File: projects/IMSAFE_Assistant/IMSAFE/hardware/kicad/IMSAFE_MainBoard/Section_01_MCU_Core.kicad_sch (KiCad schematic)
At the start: 0 parts

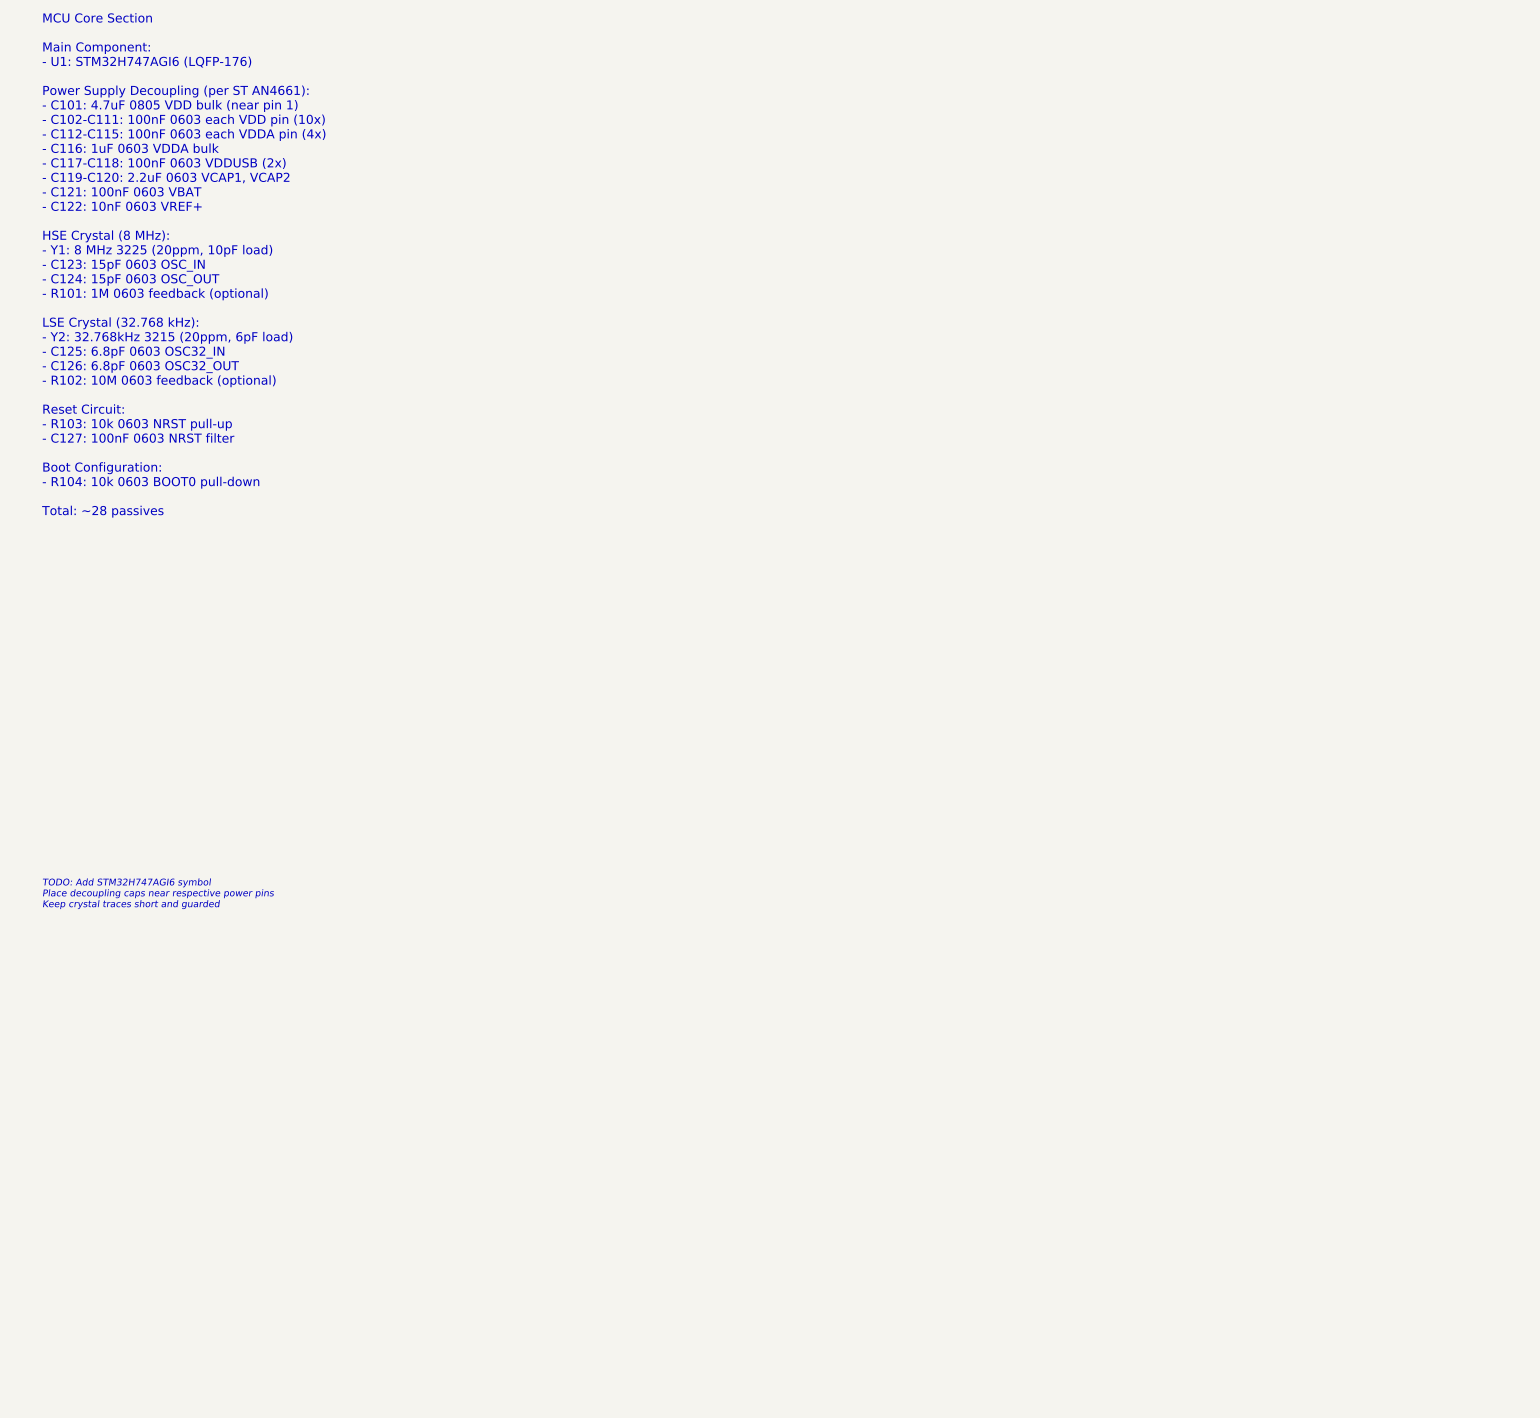
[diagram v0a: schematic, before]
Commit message: Add schematic circuits for MCU, USB-C, and Charger sections
Section 01 (MCU Core):
- STM32H747 decoupling network (22 caps per AN4661)
- HSE 8MHz and LSE 32.768kHz crystal circuits
- Reset circuit with pull-up and filter
- BOOT0 pull-down for flash boot

Section 02 (USB-C Input):
- USB-C 16-pin receptacle with CC resistors (UFP sink)
- USBLC6-2SC6 ESD protection on D+/D-
- VBUS filtering (100nF + 10uF)

Section 03 (Battery Charger):
- BQ25792 buck-boost charger with NVDC power-path
- 2.2uH power inductor
- Input, output, and system capacitors
- Current sense resistors and I2C pull-ups

Co-Authored-By: Claude Opus 4.5 <noreply@anthropic.com>
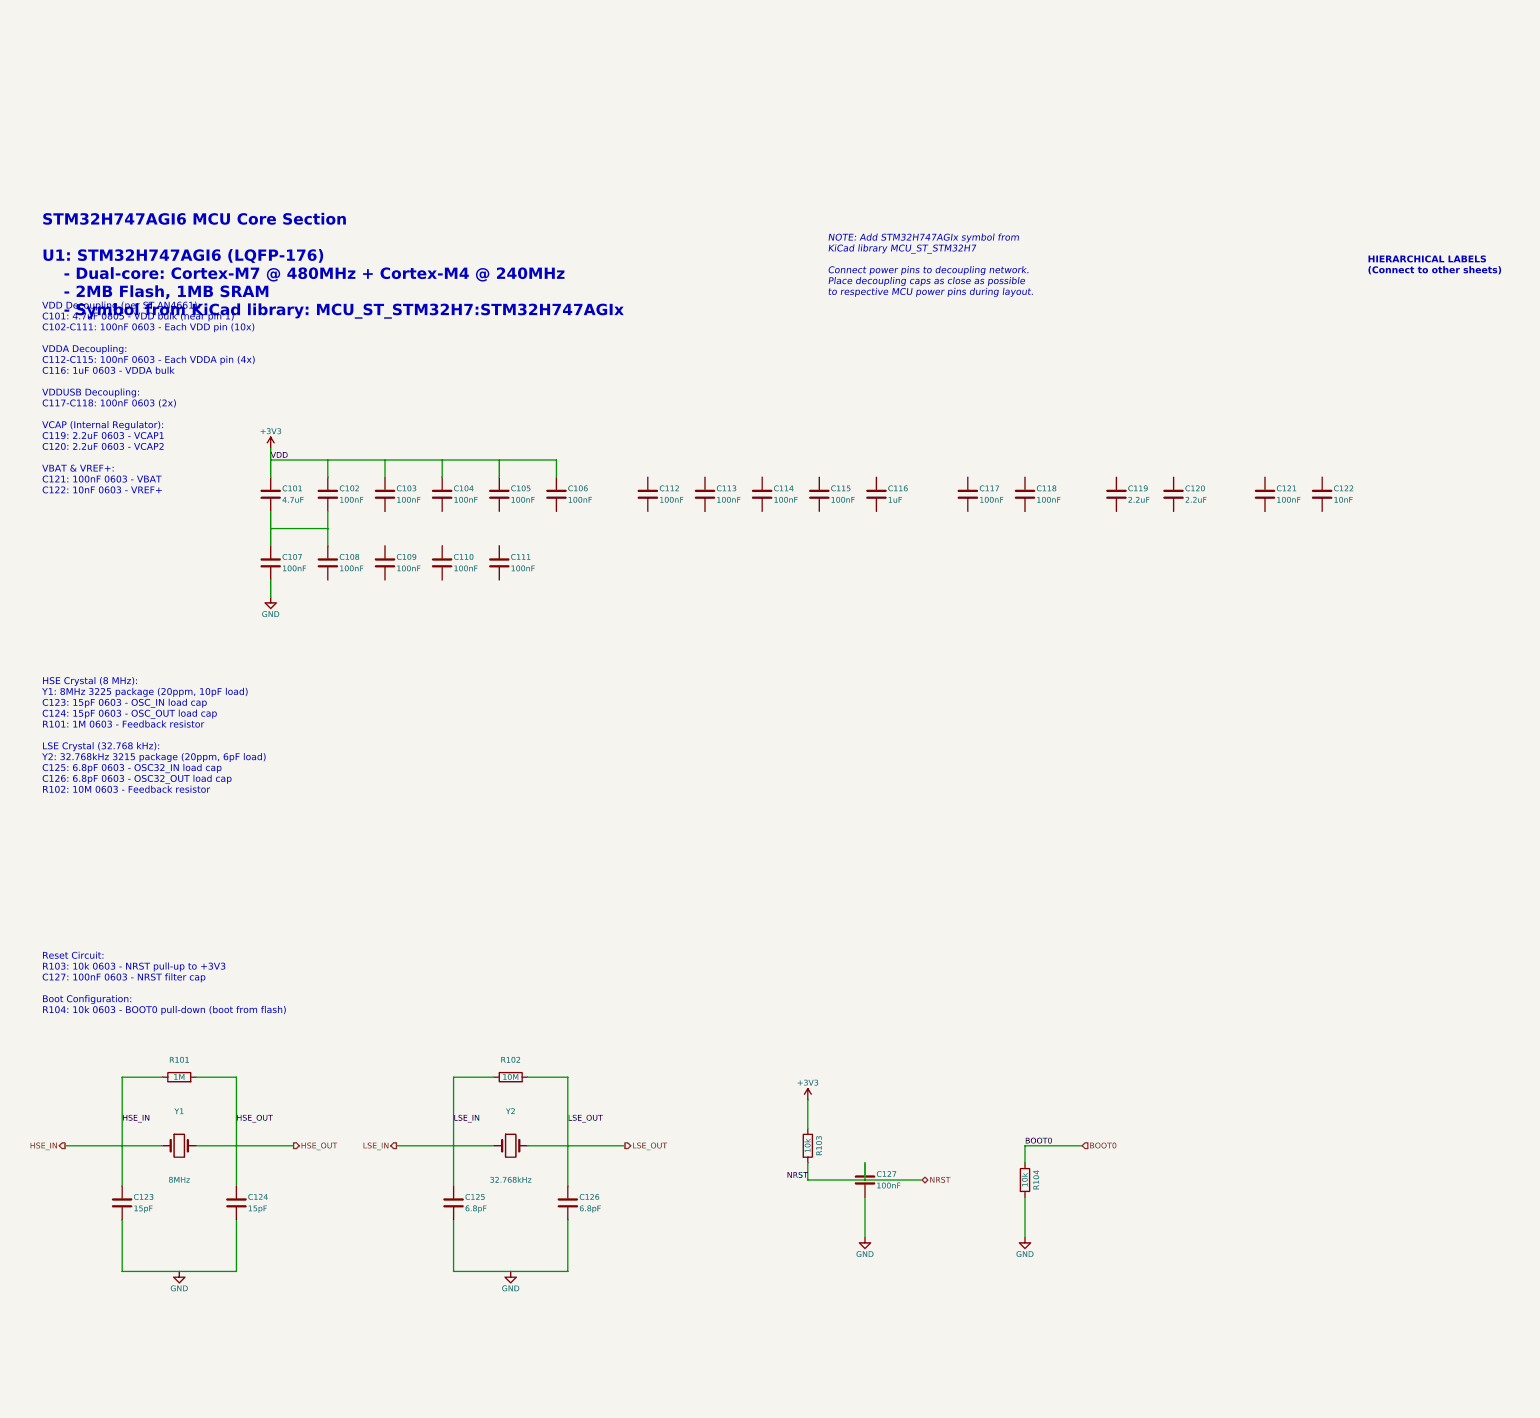
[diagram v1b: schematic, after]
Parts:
- added C101: 4.7uF, Capacitor_SMD:C_0805_2012Metric, symbol Device:C
- added C102, C103, C104, C105, C106, C107, C108, C109, C110, C111, C112, C113, C114, C115, C117, C118, C121, C127: 100nF, Capacitor_SMD:C_0603_1608Metric, symbol Device:C
- added C116: 1uF, Capacitor_SMD:C_0603_1608Metric, symbol Device:C
- added C119, C120: 2.2uF, Capacitor_SMD:C_0603_1608Metric, symbol Device:C
- added C122: 10nF, Capacitor_SMD:C_0603_1608Metric, symbol Device:C
- added C123, C124: 15pF, Capacitor_SMD:C_0603_1608Metric, symbol Device:C
- added C125, C126: 6.8pF, Capacitor_SMD:C_0603_1608Metric, symbol Device:C
- added R101: 1M, Resistor_SMD:R_0603_1608Metric, symbol Device:R
- added R102: 10M, Resistor_SMD:R_0603_1608Metric, symbol Device:R
- added R103, R104: 10k, Resistor_SMD:R_0603_1608Metric, symbol Device:R
- added Y1: 8MHz, Crystal:Crystal_SMD_3225-4Pin_3.2x2.5mm, symbol Device:Crystal
- added Y2: 32.768kHz, Crystal:Crystal_SMD_3215-2Pin_3.2x1.5mm, symbol Device:Crystal
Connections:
- new net: C101.2, C102.2, C107.1, C108.1
- new net +3V3: C101.1, C106.1, R103.1
- new net BOOT0: R104.1
- new net GND: C107.2, C123.2, C124.2, C125.2, C126.2, C127.2, R104.2
- new net HSE_IN: C123.1, R101.1, Y1.1
- new net HSE_OUT: C124.1, R101.2, Y1.2
- new net LSE_IN: C125.1, R102.1, Y2.1
- new net LSE_OUT: C126.1, R102.2, Y2.2
- new net NRST: C127.1, R103.2
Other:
- note added: "HIERARCHICAL LABELS (Connect to other sheets)"
- note added: "HSE Crystal (8 MHz): Y1: 8MHz 3225 package (20ppm, 10pF load) C123: 15pF 0603 - OSC_IN load cap C124: 15pF 0603 - OSC_OUT load cap R101: 1M 0603 - Feedback resistor LSE Crystal (32.768 kHz): Y2: 32.768kHz 3215 package (20ppm, 6pF load) C125: 6.8pF 0603 - OSC32_IN load cap C126: 6.8pF 0603 - OSC32_OUT load cap R102: 10M 0603 - Feedback resistor"
- note added: "NOTE: Add STM32H747AGIx symbol from KiCad library MCU_ST_STM32H7 Connect power pins to decoupling network. Place decoupling caps as close as possible to respective MCU power pins during layout."
- note added: "Reset Circuit: R103: 10k 0603 - NRST pull-up to +3V3 C127: 100nF 0603 - NRST filter cap Boot Configuration: R104: 10k 0603 - BOOT0 pull-down (boot from flash)"
- note added: "STM32H747AGI6 MCU Core Section U1: STM32H747AGI6 (LQFP-176) - Dual-core: Cortex-M7 @ 480MHz + Cortex-M4 @ 240MHz - 2MB Flash, 1MB SRAM - Symbol from KiCad library: MCU_ST_STM32H7:STM32H747AGIx"
- note added: "VDD Decoupling (per ST AN4661): C101: 4.7uF 0805 - VDD bulk (near pin 1) C102-C111: 100nF 0603 - Each VDD pin (10x) VDDA Decoupling: C112-C115: 100nF 0603 - Each VDDA pin (4x) C116: 1uF 0603 - VDDA bulk VDDUSB Decoupling: C117-C118: 100nF 0603 (2x) VCAP (Internal Regulator): C119: 2.2uF 0603 - VCAP1 C120: 2.2uF 0603 - VCAP2 VBAT & VREF+: C121: 100nF 0603 - VBAT C122: 10nF 0603 - VREF+"
- note removed: "MCU Core Section Main Component: - U1: STM32H747AGI6 (LQFP-176) Power Supply Decoupling (per ST AN4661): - C101: 4.7uF 0805 VDD bulk (near pin 1) - C102-C111: 100nF 0603 each VDD pin (10x) - C112-C115: 100nF 0603 each VDDA pin (4x) - C116: 1uF 0603 VDDA bulk - C117-C118: 100nF 0603 VDDUSB (2x) - C119-C120: 2.2uF 0603 VCAP1, VCAP2 - C121: 100nF 0603 VBAT - C122: 10nF 0603 VREF+ HSE Crystal (8 MHz)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"
- note removed: "TODO: Add STM32H747AGI6 symbol Place decoupling caps near respective power pins Keep crystal traces short and guarded"

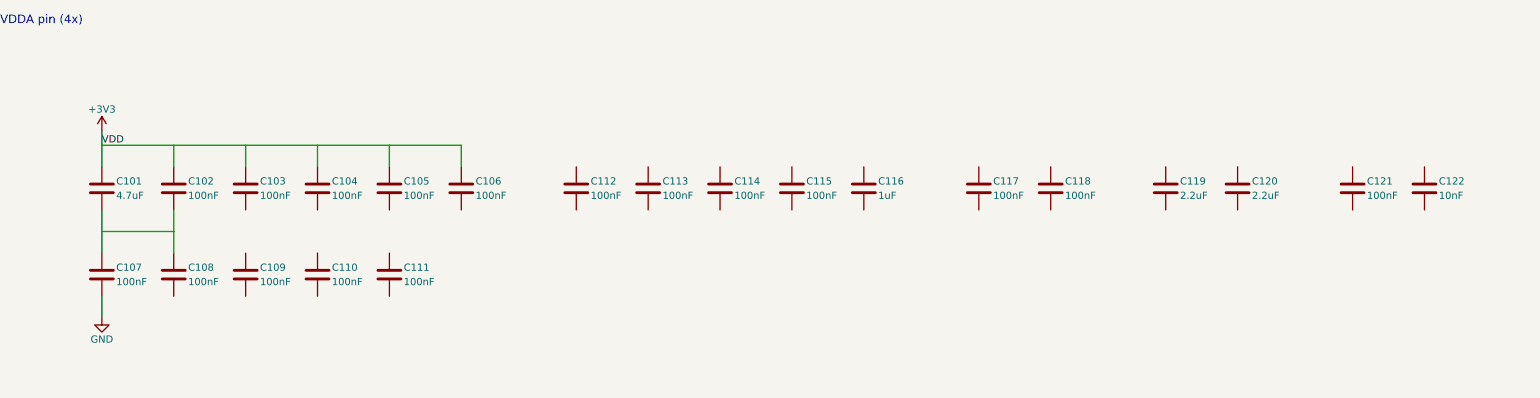
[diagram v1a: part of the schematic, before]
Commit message: Add sensor and interface schematic implementations
- Section 01: MCU Core additional connections
- Section 04: BMS refinements
- Section 07: Barometric sensor (BMP390)
- Section 08: IMU (ICM-42688-P) full implementation
- Section 09: Magnetometer (MMC5983MA) full implementation
- Section 10: Gas sensor (MICS-4514) with heater control
- Section 11: Temp/Humidity (Si7021-A20) implementation
- Section 14: I/O Expander updates
- Section 16: Rotary encoder connections
- Section 19: Audio buzzer (MLT-8530) with MOSFET driver

Co-Authored-By: Claude Opus 4.5 <noreply@anthropic.com>
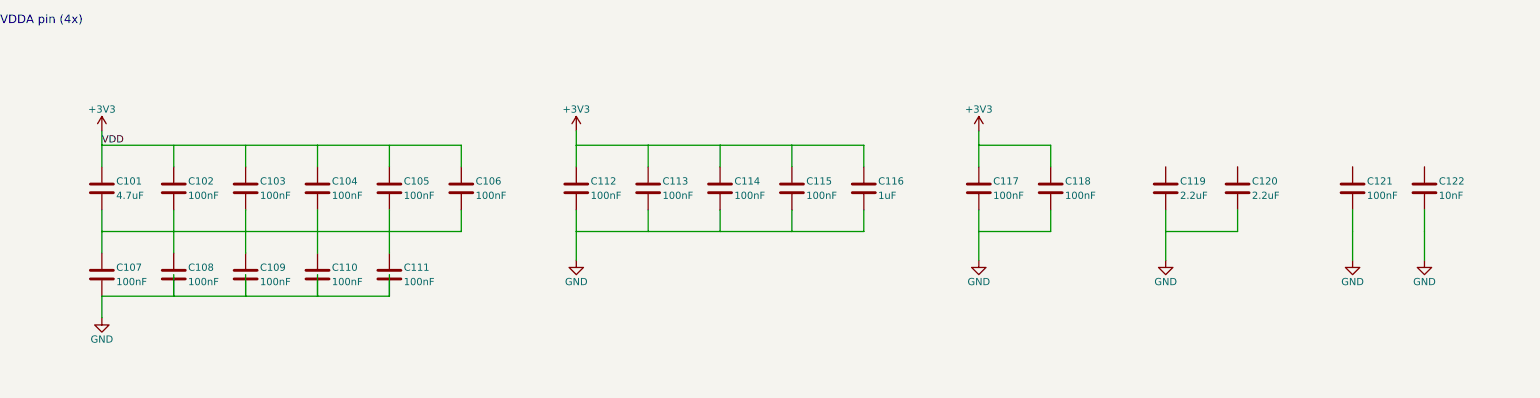
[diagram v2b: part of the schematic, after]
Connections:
- net +3V3: now also C112.1, C113.1, C114.1, C115.1, C116.1, C117.1, C118.1
- net GND: now also C108.2, C109.2, C110.2, C111.2, C112.2, C113.2, C114.2, C115.2, C116.2, C117.2, C118.2, C119.2, C120.2, C121.2, C122.2
- net at C101.2, C102.2, C107.1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: now also C103.2, C104.2, C105.2, C106.2, C109.1, C110.1, C111.1

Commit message: Update KiCad schematics and add analysis files
- Update all MainBoard schematic sections with component placement
- Add ERC reports and analysis scripts for schematic validation
- Update Radar Interface and SwitchLED Board projects
- Sync KiCad project files with latest session changes

Co-Authored-By: Claude Opus 4.5 <noreply@anthropic.com>
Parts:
- removed C101: 4.7uF, Capacitor_SMD:C_0805_2012Metric, symbol Device:C
- removed C102, C103, C104, C105, C106, C107, C108, C109, C110, C111, C112, C113, C114, C115, C117, C118, C121, C127: 100nF, Capacitor_SMD:C_0603_1608Metric, symbol Device:C
- removed C116: 1uF, Capacitor_SMD:C_0603_1608Metric, symbol Device:C
- removed C119, C120: 2.2uF, Capacitor_SMD:C_0603_1608Metric, symbol Device:C
- removed C122: 10nF, Capacitor_SMD:C_0603_1608Metric, symbol Device:C
- removed C123, C124: 15pF, Capacitor_SMD:C_0603_1608Metric, symbol Device:C
- removed C125, C126: 6.8pF, Capacitor_SMD:C_0603_1608Metric, symbol Device:C
- removed R101: 1M, Resistor_SMD:R_0603_1608Metric, symbol Device:R
- removed R102: 10M, Resistor_SMD:R_0603_1608Metric, symbol Device:R
- removed R103, R104: 10k, Resistor_SMD:R_0603_1608Metric, symbol Device:R
- removed Y1: 8MHz, Crystal:Crystal_SMD_3225-4Pin_3.2x2.5mm, symbol Device:Crystal
- removed Y2: 32.768kHz, Crystal:Crystal_SMD_3215-2Pin_3.2x1.5mm, symbol Device:Crystal
- added C? (x2): 6.8pF, Capacitor_SMD:C_0603_1608Metric, symbol Device:C
- added C? (x18): 100nF, Capacitor_SMD:C_0603_1608Metric, symbol Device:C
- added C? (x2): 2.2uF, Capacitor_SMD:C_0603_1608Metric, symbol Device:C
- added C?: 10nF, Capacitor_SMD:C_0603_1608Metric, symbol Device:C
- added C?: 1uF, Capacitor_SMD:C_0603_1608Metric, symbol Device:C
- added C?: 4.7uF, Capacitor_SMD:C_0805_2012Metric, symbol Device:C
- added C? (x2): 15pF, Capacitor_SMD:C_0603_1608Metric, symbol Device:C
- added R?: 1M, Resistor_SMD:R_0603_1608Metric, symbol Device:R
- added R? (x2): 10k, Resistor_SMD:R_0603_1608Metric, symbol Device:R
- added R?: 10M, Resistor_SMD:R_0603_1608Metric, symbol Device:R
- added U2: STM32H747IIT6, LQFP-176, symbol 1_New_library:STM32H747IIT6
- added Y?: 32.768kHz, Crystal:Crystal_SMD_3215-2Pin_3.2x1.5mm, symbol Device:Crystal
- added Y?: 8MHz, Crystal:Crystal_SMD_3225-4Pin_3.2x2.5mm, symbol Device:Crystal
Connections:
- net +3V3: now also C?.1, C?.1, C?.1, C?.1, C?.1, C?.1, C?.1, C?.1, C?.1, C?.1, C?.1, C?.1, C?.1, R?.1
- net BOOT0: now also R?.1
- net GND: now also C?.2, C?.2, C?.2, C?.2, C?.2, C?.2, C?.2, C?.2, C?.2, C?.2, C?.2, C?.2, C?.2, C?.2, C?.2, C?.2, C?.2, C?.2, C?.2, C?.2, C?.2, R?.2
- net HSE_IN: now also C?.1, R?.1, Y?.1
- net HSE_OUT: now also C?.1, R?.2, Y?.2
- net LSE_IN: now also C?.1, R?.1, Y?.1
- net LSE_OUT: now also C?.1, R?.2, Y?.2
- net NRST: now also C?.1, R?.2
- new net: C?.1, C?.1, C?.1, C?.1, C?.1, C?.2, C?.2, C?.2, C?.2, C?.2, C?.2
